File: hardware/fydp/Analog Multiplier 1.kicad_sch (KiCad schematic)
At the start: 26 parts, among them J8 Conn_01x02_Pin, U10 LTC2630ISC6-LZ8-TRMPBF, U11 SN74LVC1G3157DCKR, U12 AD633ARZ-R7, U13 LTC2630ISC6-LZ8-TRMPBF, U14 SN74LVC1G3157DCKR, U15 AD633ARZ-R7

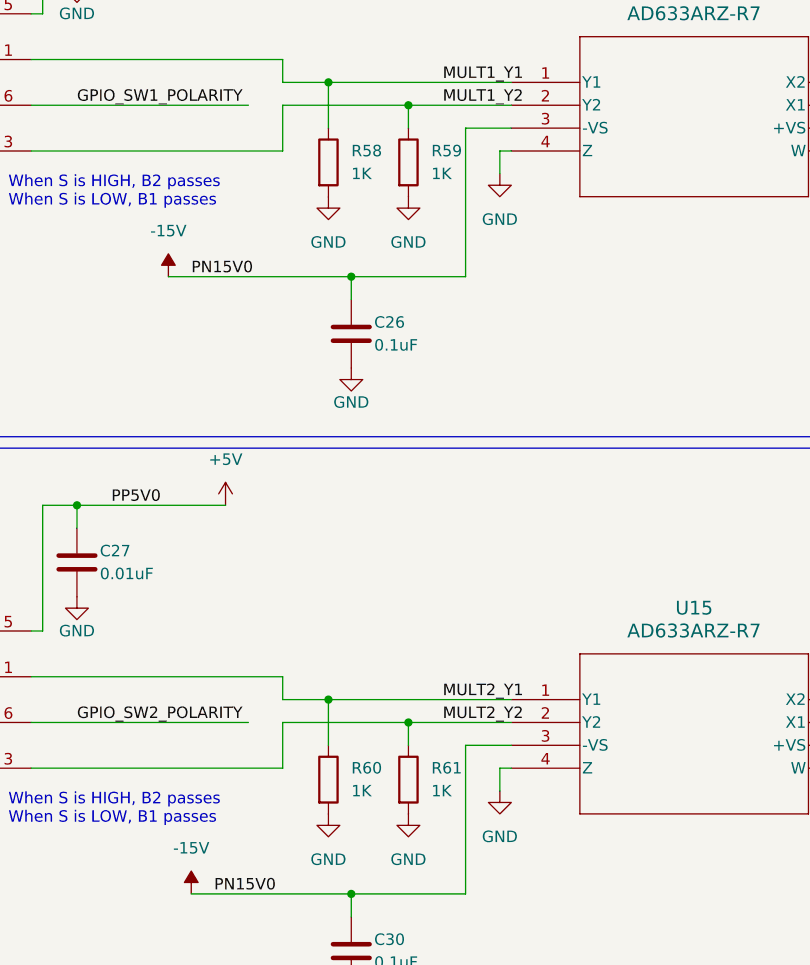
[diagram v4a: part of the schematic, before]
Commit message: Adding JLCPCB BOM notes
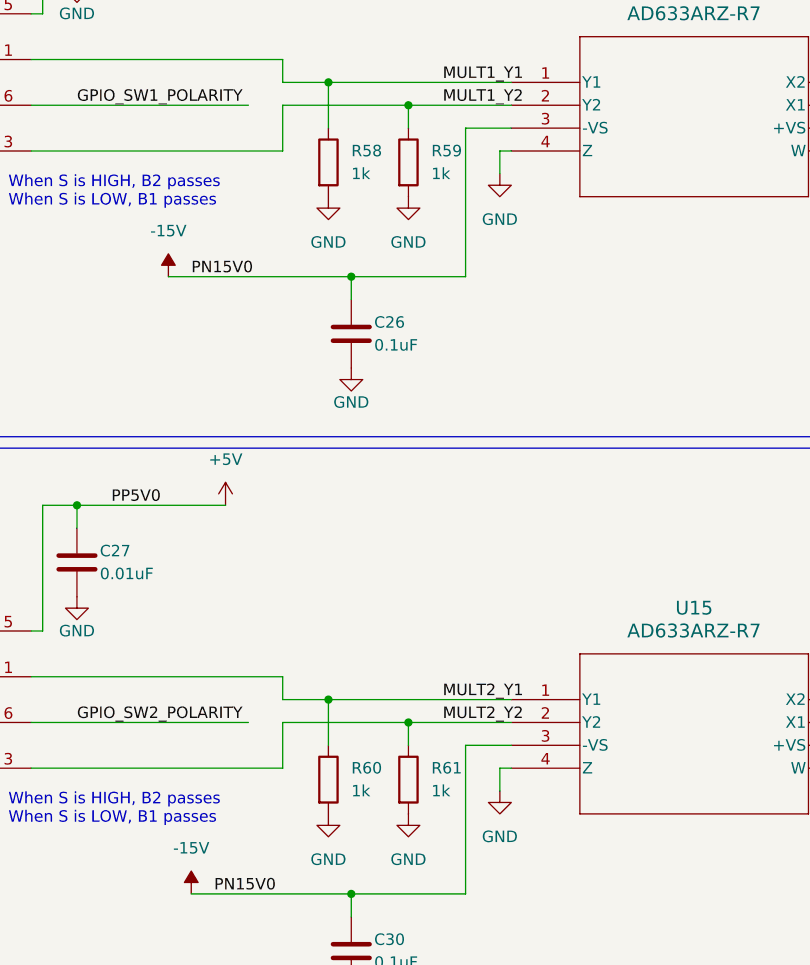
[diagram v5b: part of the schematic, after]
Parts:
- C23, C27: Comment (none) -> 10000 pF ±10% 50V Ceramic Capacitor X7R 0805 (2012 Metric); LCSC (none) -> C83170; MPN (none) -> CC0805KRX7R9BB103
- C24, C25, C26, C28, C29, C30: Comment (none) -> 0.1 µF ±10% 50V Ceramic Capacitor X7R 0805 (2012 Metric); LCSC (none) -> C49678; MPN (none) -> CC0805KRX7R9BB104
- R52: Comment (none) -> 100 Ohms ±1% 0.125W, 1/8W Chip Resistor 0805 (2012 Metric) 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; LCSC (none) -> C105577; MPN (none) -> RC0805FR-07100RL
- R58, R59, R60, R61: value 1K -> 1k; Comment (none) -> 1 kOhms ±1% 0.125W, 1/8W Chip Resistor 0805 (2012 Metric) M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; LCSC (none) -> C95781; MPN (none) -> RC0805FR-071KL

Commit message: Updating BOM some more
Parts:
- J8: Comment (none) -> Connector Header Through Hole 2 position 0.100" (2.54mm); MPN (none) -> TSW-102-07-G-S
- U10, U13: Comment (none) -> 8 Bit Digital to Analog Converter 1 SC-70-6; MPN (none) -> LTC2630ISC6-LZ8#TRMPBF
- U11, U14: Comment (none) -> 1 Circuit IC Switch 2:1 15Ohm SC-70-6; LCSC (none) -> C38663; MPN (none) -> SN74LVC1G3157DCKR
- U12, U15: Comment (none) -> Analog Multiplier 4-Quadrant 8-SOIC; LCSC (none) -> C77810; MPN (none) -> AD633ARZ-R7
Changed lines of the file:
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@@
       (effects (font (size 1.27 1.27)) hide)
     )
-    (property "Datasheet" "~" (at 27.94 184.15 0)
+    (property "Datasheet" "https://suddendocs.samtec.com/catalog_english/tsw_th.pdf" (at 27.94 184.15 0)
+      (effects (font (size 1.27 1.27)) hide)
+    )
+    (property "Comment" "Connector Header Through Hole 2 position 0.100\" (2.54mm)" (at 27.94 184.15 0)
+      (effects (font (size 1.27 1.27)) hide)
+    )
+    (property "MPN" "TSW-102-07-G-S" (at 27.94 184.15 0)
       (effects (font (size 1.27 1.27)) hide)
     )
@@
       (effects (font (size 1.27 1.27)) hide)
     )
-    (property "Datasheet" "~" (at 97.79 184.15 0)
+    (property "Datasheet" "https://suddendocs.samtec.com/catalog_english/tsw_th.pdf" (at 97.79 184.15 0)
+      (effects (font (size 1.27 1.27)) hide)
+    )
+    (property "Comment" "Connector Header Through Hole 2 position 0.100\" (2.54mm)" (at 97.79 184.15 0)
+      (effects (font (size 1.27 1.27)) hide)
+    )
+    (property "MPN" "TSW-102-07-G-S" (at 97.79 184.15 0)
       (effects (font (size 1.27 1.27)) hide)
     )
@@
       (effects (font (size 1.27 1.27) italic) hide)
     )
-    (property "Datasheet" "LTC2630ISC6-LZ8-TRMPBF" (at 35.56 48.26 0)
+    (property "Datasheet" "https://www.analog.com/media/en/technical-documentation/data-sheets/2630fg.pdf" (at 35.56 48.26 0)
       (effects (font (size 1.27 1.27) italic) hide)
+    )
+    (property "Comment" "8 Bit Digital to Analog Converter 1 SC-70-6" (at 35.56 48.26 0)
+      (effects (font (size 1.27 1.27)) hide)
+    )
+    (property "MPN" "LTC2630ISC6-LZ8#TRMPBF" (at 35.56 48.26 0)
+      (effects (font (size 1.27 1.27)) hide)
     )
     (pin "1")
@@
       (effects (font (size 1.27 1.27) italic) hide)
     )
-    (property "Datasheet" "AD633ARZ-R7" (at 198.12 124.46 0)
+    (property "Datasheet" "https://www.analog.com/media/en/technical-documentation/data-sheets/AD633.pdf" (at 198.12 124.46 0)
       (effects (font (size 1.27 1.27) italic) hide)
+    )
+    (property "Comment" "Analog Multiplier 4-Quadrant 8-SOIC" (at 198.12 124.46 0)
+      (effects (font (size 1.27 1.27)) hide)
+    )
+    (property "LCSC" "C77810" (at 198.12 124.46 0)
+      (effects (font (size 1.27 1.27)) hide)
+    )
+    (property "MPN" "AD633ARZ-R7" (at 198.12 124.46 0)
+      (effects (font (size 1.27 1.27)) hide)
     )
     (pin "1")
@@
       (effects (font (size 1.27 1.27) italic) hide)
     )
-    (property "Datasheet" "LTC2630ISC6-LZ8-TRMPBF" (at 35.56 116.84 0)
+    (property "Datasheet" "https://www.analog.com/media/en/technical-documentation/data-sheets/2630fg.pdf" (at 35.56 116.84 0)
       (effects (font (size 1.27 1.27) italic) hide)
+    )
+    (property "Comment" "8 Bit Digital to Analog Converter 1 SC-70-6" (at 35.56 116.84 0)
+      (effects (font (size 1.27 1.27)) hide)
+    )
+    (property "MPN" "LTC2630ISC6-LZ8#TRMPBF" (at 35.56 116.84 0)
+      (effects (font (size 1.27 1.27)) hide)
     )
     (pin "1")
@@
       (effects (font (size 1.27 1.27) italic) hide)
     )
-    (property "Datasheet" "SN74LVC1G3157DCKR" (at 121.92 124.46 0)
+    (property "Datasheet" "https://www.ti.com/general/docs/suppproductinfo.tsp?distId=10&gotoUrl=https%3A%2F%2Fwww.ti.com%2Flit%2Fgpn%2Fsn74lvc1g3157" (at 121.92 124.46 0)
       (effects (font (size 1.27 1.27) italic) hide)
+    )
+    (property "Comment" "1 Circuit IC Switch 2:1 15Ohm SC-70-6" (at 121.92 124.46 0)
+      (effects (font (size 1.27 1.27)) hide)
+    )
+    (property "LCSC" "C38663" (at 121.92 124.46 0)
+      (effects (font (size 1.27 1.27)) hide)
+    )
+    (property "MPN" "SN74LVC1G3157DCKR" (at 121.92 124.46 0)
+      (effects (font (size 1.27 1.27)) hide)
     )
     (pin "1")
@@
       (effects (font (size 1.27 1.27) italic) hide)
     )
-    (property "Datasheet" "SN74LVC1G3157DCKR" (at 121.92 55.88 0)
+    (property "Datasheet" "https://www.ti.com/general/docs/suppproductinfo.tsp?distId=10&gotoUrl=https%3A%2F%2Fwww.ti.com%2Flit%2Fgpn%2Fsn74lvc1g3157" (at 121.92 55.88 0)
       (effects (font (size 1.27 1.27) italic) hide)
+    )
+    (property "Comment" "1 Circuit IC Switch 2:1 15Ohm SC-70-6" (at 121.92 55.88 0)
+      (effects (font (size 1.27 1.27)) hide)
+    )
+    (property "LCSC" "C38663" (at 121.92 55.88 0)
+      (effects (font (size 1.27 1.27)) hide)
+    )
+    (property "MPN" "SN74LVC1G3157DCKR" (at 121.92 55.88 0)
+      (effects (font (size 1.27 1.27)) hide)
     )
     (pin "1")
@@
       (effects (font (size 1.27 1.27) italic) hide)
     )
-    (property "Datasheet" "AD633ARZ-R7" (at 198.12 55.88 0)
+    (property "Datasheet" "https://www.analog.com/media/en/technical-documentation/data-sheets/AD633.pdf" (at 198.12 55.88 0)
       (effects (font (size 1.27 1.27) italic) hide)
     )
-    (pin "1")
+    (property "Comment" "Analog Multiplier 4-Quadrant 8-SOIC" (at 198.12 55.88 0)
+      (effects (font (size 1.27 1.27)) hide)
+    )
+    (property "LCSC" "C77810" (at 198.12 55.88 0)
+      (effects (font (size 1.27 1.27)) hide)
+    )
+    (property "MPN" "AD633ARZ-R7" (at 198.12 55.88 0)
+      (effects (font (size 1.27 1.27)) hide)
+    )
+    (pin "1")

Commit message: Pushing laptop changes
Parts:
- U10, U13: value LTC2630ISC6-LZ8-TRMPBF -> LTC2630ISC6-HZ12#TRMPBF; Comment 8 Bit Digital to Analog Converter 1 SC-70-6 -> 12 Bit Digital to Analog Converter 1 SC-70-6; MPN LTC2630ISC6-LZ8#TRMPBF -> LTC2630ISC6-HZ12#TRMPBF
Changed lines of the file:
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@@
       (effects (font (size 1.524 1.524)))
     )
-    (property "Value" "LTC2630ISC6-LZ8-TRMPBF" (at 58.42 40.64 0)
+    (property "Value" "LTC2630ISC6-HZ12#TRMPBF" (at 58.42 40.64 0)
       (effects (font (size 1.524 1.524)))
     )
@@
       (effects (font (size 1.27 1.27) italic) hide)
     )
-    (property "Comment" "8 Bit Digital to Analog Converter 1 SC-70-6" (at 35.56 48.26 0)
+    (property "Comment" "12 Bit Digital to Analog Converter 1 SC-70-6" (at 35.56 48.26 0)
       (effects (font (size 1.27 1.27)) hide)
     )
-    (property "MPN" "LTC2630ISC6-LZ8#TRMPBF" (at 35.56 48.26 0)
+    (property "MPN" "LTC2630ISC6-HZ12#TRMPBF" (at 35.56 48.26 0)
       (effects (font (size 1.27 1.27)) hide)
     )
@@
       (effects (font (size 1.524 1.524)))
     )
-    (property "Value" "LTC2630ISC6-LZ8-TRMPBF" (at 58.42 109.22 0)
+    (property "Value" "LTC2630ISC6-HZ12#TRMPBF" (at 58.42 109.22 0)
       (effects (font (size 1.524 1.524)))
     )
@@
       (effects (font (size 1.27 1.27) italic) hide)
     )
-    (property "Comment" "8 Bit Digital to Analog Converter 1 SC-70-6" (at 35.56 116.84 0)
+    (property "Comment" "12 Bit Digital to Analog Converter 1 SC-70-6" (at 35.56 116.84 0)
       (effects (font (size 1.27 1.27)) hide)
     )
-    (property "MPN" "LTC2630ISC6-LZ8#TRMPBF" (at 35.56 116.84 0)
+    (property "MPN" "LTC2630ISC6-HZ12#TRMPBF" (at 35.56 116.84 0)
       (effects (font (size 1.27 1.27)) hide)
     )

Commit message: Fixed footprints
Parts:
- J8: value Conn_01x02_Pin -> TSW-102-07-G-S
- U11, U14: footprint Package_TO_SOT_SMD:SOT-23-6_Handsoldering -> Package_TO_SOT_SMD:SOT-363_SC-70-6_Handsoldering
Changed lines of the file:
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@@
       (effects (font (size 1.27 1.27)))
     )
-    (property "Value" "Conn_01x02_Pin" (at 28.575 181.61 0)
+    (property "Value" "TSW-102-07-G-S" (at 28.575 181.61 0)
       (effects (font (size 1.27 1.27)))
     )
@@
       (effects (font (size 1.27 1.27)))
     )
-    (property "Value" "Conn_01x02_Pin" (at 98.425 181.61 0)
+    (property "Value" "TSW-102-07-G-S" (at 98.425 181.61 0)
       (effects (font (size 1.27 1.27)))
     )
@@
       (effects (font (size 1.524 1.524)))
     )
-    (property "Footprint" "Package_TO_SOT_SMD:SOT-23-6_Handsoldering" (at 121.92 124.46 0)
+    (property "Footprint" "Package_TO_SOT_SMD:SOT-363_SC-70-6_Handsoldering" (at 121.92 124.46 0)
       (effects (font (size 1.27 1.27) italic) hide)
     )
@@
       (effects (font (size 1.524 1.524)))
     )
-    (property "Footprint" "Package_TO_SOT_SMD:SOT-23-6_Handsoldering" (at 121.92 55.88 0)
+    (property "Footprint" "Package_TO_SOT_SMD:SOT-363_SC-70-6_Handsoldering" (at 121.92 55.88 0)
       (effects (font (size 1.27 1.27) italic) hide)
     )
